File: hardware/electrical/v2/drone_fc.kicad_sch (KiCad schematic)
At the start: 33 parts, among them J1 Cortex_SWD_10P, J2 ESC_4IN1_JST_SH, U1 TLV75533PDBVR, U2 LMR50410_Buck, U3 MDBT53-P1M, U4 ICM-42688-P

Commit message: j2: adopt the KiCad library footprint for the ESC connector
Switches J2 from the hand-made drone_fc_v2_footprints copy to KiCad's
Connector_JST:JST_SH_SM08B-SRSS-TB_1x08-1MP_P1.00mm_Horizontal.

The two disagreed on the mechanical retention pads: signal-to-MP separation
of 3.25 mm against 3.875 mm, with the MP pads 0.4 mm further out in the
library version. Those pads take the load every time the ESC harness is
unplugged, so the geometry matters. JST's own drawing could not be read
programmatically to arbitrate, but provenance is decisive - the library
footprint is machine-generated from eSH.pdf by kicad-footprint-generator and
peer-reviewed, whereas ours came from the same CopperPilot generation that
produced mislabelled symbol pins, a self-intersecting courtyard and an
unverified BOM. The swap also brings the manufacturer STEP model, which the
custom footprint lacked.

Also links TP1-TP4 to their schematic symbols. Those pads were created
directly in the board file before the matching TestPoint symbols existed, so
they carried no path and Update PCB from Schematic kept offering to add four
duplicates.

This is an intermediate state with known errors. Fitting the reviewed
footprint revealed that the connector opens toward the board centre rather
than out through the edge, so it still needs rotating 180 degrees and moving
to y ~88.6. Until then DRC reports eight board-edge clearance errors (pads
0.425 mm from the edge against a 0.5 mm rule) and a courtyard overlap with
TP2, all within the area that rework will cover. ERC is clean and no nets
are unconnected.
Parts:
- J2: footprint drone_fc_v2_footprints:JST_SH_SM08B-SRSS-TB_1x08-1MP_P1.00mm_Horizontal -> Connector_JST:JST_SH_SM08B-SRSS-TB_1x08-1MP_P1.00mm_Horizontal
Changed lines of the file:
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@@
 			)
 		)
-		(property "Footprint" "drone_fc_v2_footprints:JST_SH_SM08B-SRSS-TB_1x08-1MP_P1.00mm_Horizontal"
+		(property "Footprint" "Connector_JST:JST_SH_SM08B-SRSS-TB_1x08-1MP_P1.00mm_Horizontal"
 			(at 342.9 195.58 0)
 			(hide yes)

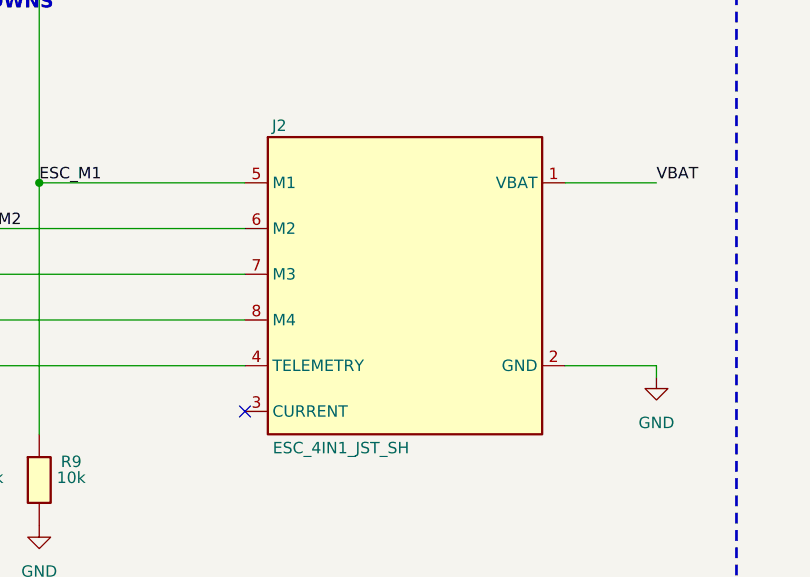
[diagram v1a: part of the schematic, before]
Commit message: j2: reverse connector pin numbering to match the ESC harness
The board-side pinout is now pin 1 = M4 through pin 8 = VBAT, reversed from
the JST convention the parts-list documents. This matches the custom harness
as measured: with the socket held open-end toward you, VBAT sits on the right,
which places it on the left-hand pad once the header is rotated to open
outward. Pin numbering is reversed in the symbol rather than the footprint, so
the schematic drawing and its wiring are unchanged and only the pad mapping
moves.

J2 is rotated 180 degrees so the connector opens out through the top board
edge rather than into the board interior. The opening direction was settled by
rendering the manufacturer STEP model - the 2D pads and courtyard are
ambiguous, and reasoning from them produced two wrong conclusions before the
render.

Intermediate state. Re-routing around the rotated connector is unfinished:
three nets are open in the buck area (+4V, C5 ground, R2 feedback) and both J2
mounting pads sit 0.235 mm from the board edge against a 0.5 mm rule, so the
connector needs nudging inboard. ERC is clean and the remaining twelve DRC
findings are silkscreen only.

Committed mid-edit because KiCad crashed; the files were checked for damage
first and both parse cleanly.
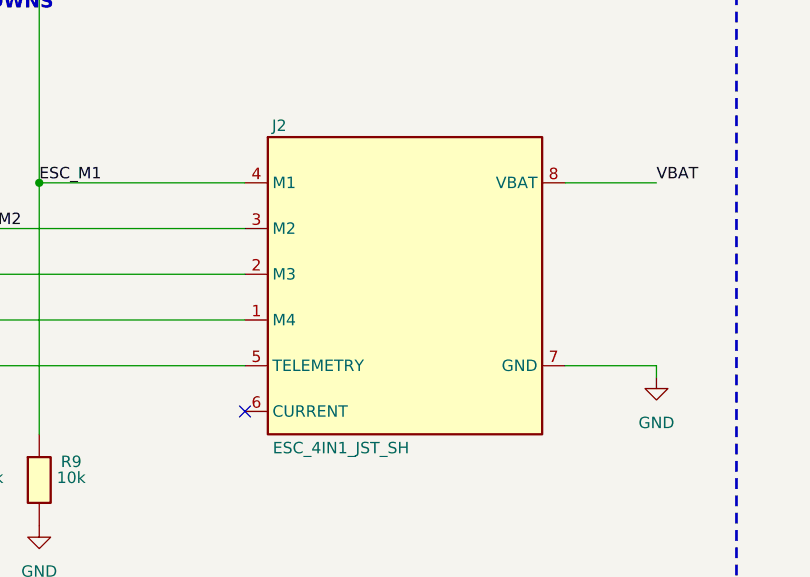
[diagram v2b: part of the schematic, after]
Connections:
- net ESC_M1: now also J2.4 (M1); no longer J2.5 (M1)
- net ESC_M2: now also J2.3 (M2); no longer J2.6 (M2)
- net ESC_M3: now also J2.2 (M3); no longer J2.7 (M3)
- net ESC_M4: now also J2.1 (M4); no longer J2.8 (M4)
- net ESC_TLM: now also J2.5 (TELEMETRY); no longer J2.4 (TELEMETRY)
- net GND: now also J2.7 (GND); no longer J2.2 (GND)
- net VBAT: now also J2.8 (VBAT); no longer J2.1 (VBAT)

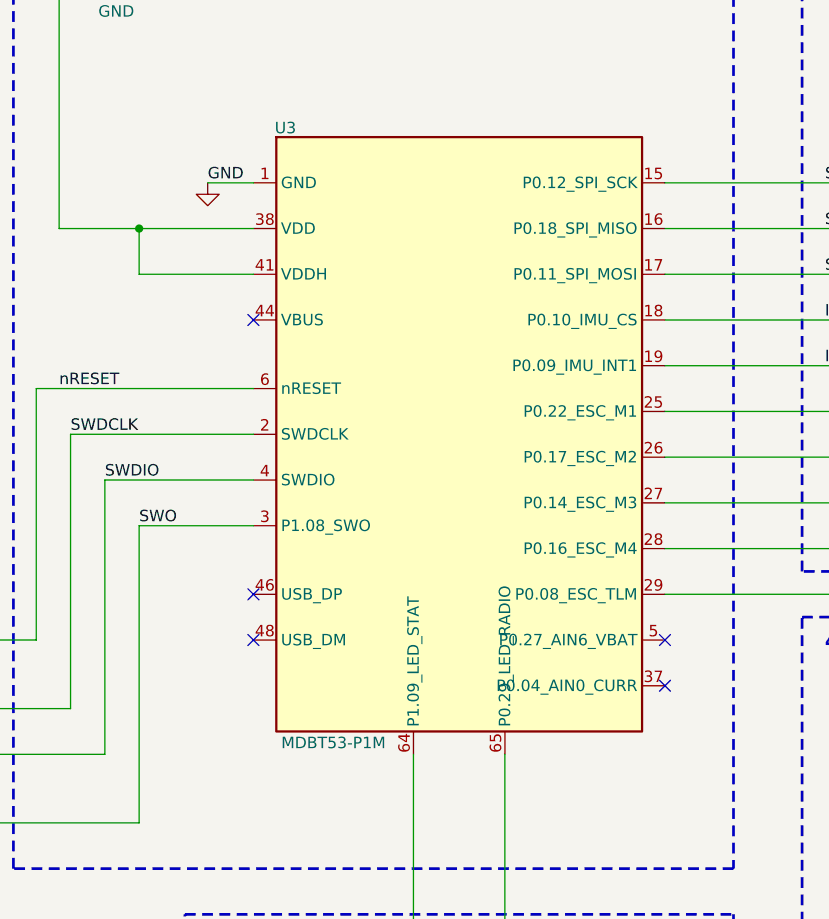
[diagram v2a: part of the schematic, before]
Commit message: u3,j2: fix pin assignments, reroute, and re-center the IMU
Corrects several MDBT53/nRF5340 pin assignments against the module's
official pin table (Raytac spec section 2.5), and reroutes accordingly:

- Add the three missing GND pins (24, 42, 61) to the MDBT53_P1M symbol.
  Only pin 1 was previously declared; the other three physical ground
  pads were floating on the board. Pin 42 was first mis-added as 43
  (P1.01, a GPIO) and corrected after cross-checking the datasheet.
- Move ESC_M3/ESC_M4 off pin 27 (inconveniently interior) onto 28/30,
  fixing a resulting crossed wire: swapping the label text alone
  didn't move the connection, since these are direct point-to-point
  wires to J2, not label-joined nets - the wire geometry had to move,
  not just its annotation.
- Reverse the motor pin order on the MCU side (M1<-30, M2<-28, M3<-26,
  M4<-25) for routing convenience, without touching the J2 wiring:
  only the silicon pin driving each already-fixed destination changed.
- Move LED_STAT/LED_RADIO off pin 58 (DECR, a regulator decoupling
  pin, not GPIO) onto 60/56.
- Move SPI_SCK/MOSI/CS/INT1 off the inner castellation row onto the
  outer row (20/18/22/14), keeping MISO at 16.
- Widen the antenna keepout to the full board width per the module
  design guide, not just the antenna footprint.
- Re-center U4 (ICM-42688-P) on the board.

Board fully re-routed for the above (0 unconnected items). ERC clean.
Remaining DRC output is expected in-progress noise: two standard-library
footprint version-drift warnings (R6/R7) and courtyard/tuning notices.
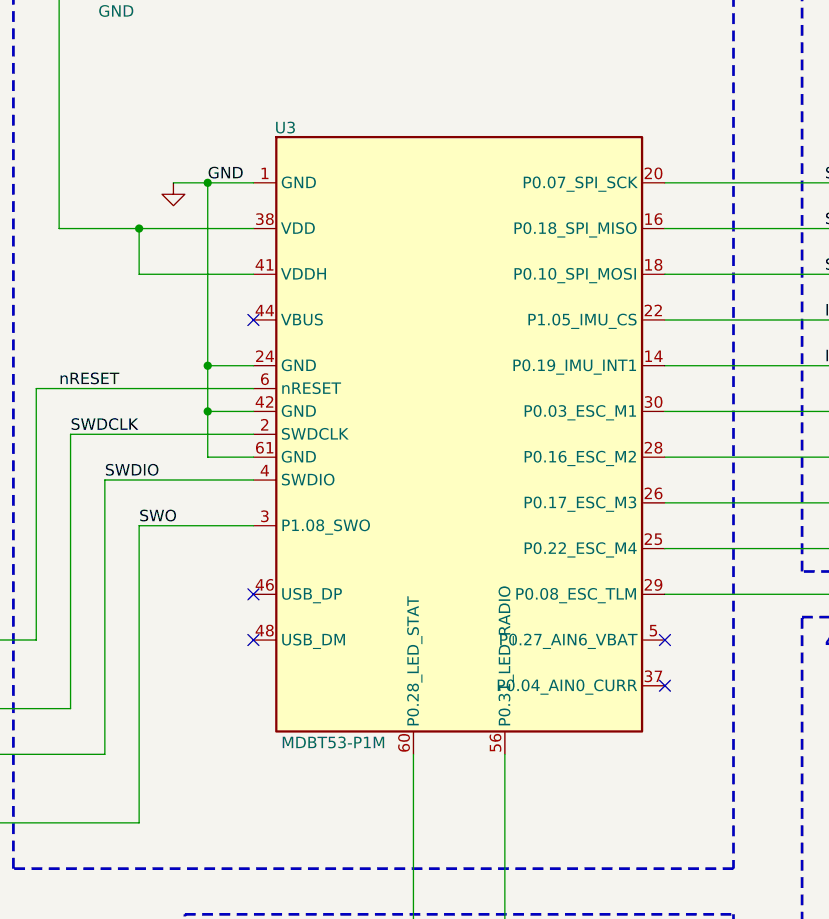
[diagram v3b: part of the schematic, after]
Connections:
- net ESC_M1: now also U3.30 (P0.03_ESC_M1); no longer U3.25 (P0.22_ESC_M1)
- net ESC_M2: now also U3.28 (P0.16_ESC_M2); no longer U3.26 (P0.17_ESC_M2)
- net ESC_M3: now also U3.26 (P0.17_ESC_M3); no longer U3.27 (P0.14_ESC_M3)
- net ESC_M4: now also U3.25 (P0.22_ESC_M4); no longer U3.28 (P0.16_ESC_M4)
- net GND: now also U3.24 (GND), U3.42 (GND), U3.61 (GND)
- net IMU_CS: now also U3.22 (P1.05_IMU_CS); no longer U3.18 (P0.10_IMU_CS)
- net IMU_INT1: now also U3.14 (P0.19_IMU_INT1); no longer U3.19 (P0.09_IMU_INT1)
- net SPI_MOSI: now also U3.18 (P0.10_SPI_MOSI); no longer U3.17 (P0.11_SPI_MOSI)
- net SPI_SCK: now also U3.20 (P0.07_SPI_SCK); no longer U3.15 (P0.12_SPI_SCK)
- net at D1.1 (A): now also U3.60 (P0.28_LED_STAT); no longer U3.64 (P1.09_LED_STAT)
- net at D2.1 (A): now also U3.56 (P0.31_LED_RADIO); no longer U3.65 (P0.29_LED_RADIO)
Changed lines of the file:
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@@
 	)
 	(junction
+		(at 187.96 139.7)
+		(diameter 0)
+		(color 0 0 0 0)
+	)
+	(junction
 		(at 360.68 129.54)
 		(diameter 0.9144)
@@
 	)
 	(junction
+		(at 187.96 134.62)
+		(diameter 0)
+		(color 0 0 0 0)
+	)
+	(junction
+		(at 187.96 114.3)
+		(diameter 0)
+		(color 0 0 0 0)
+	)
+	(junction
 		(at 373.38 129.54)
 		(diameter 0.9144)
@@
 	(wire
 		(pts
+			(xy 187.96 134.62) (xy 187.96 114.3)
+		)
+		(stroke
+			(width 0)
+			(type default)
+		)
+	)
+	(wire
+		(pts
 			(xy 350.52 137.16) (xy 360.68 137.16)
 		)
@@
 	(wire
 		(pts
+			(xy 184.15 114.3) (xy 187.96 114.3)
+		)
+		(stroke
+			(width 0)
+			(type default)
+		)
+	)
+	(wire
+		(pts
 			(xy 168.91 137.16) (xy 193.04 137.16)
 		)
@@
 	(wire
 		(pts
+			(xy 193.04 139.7) (xy 187.96 139.7)
+		)
+		(stroke
+			(width 0)
+			(type default)
+		)
+	)
+	(wire
+		(pts
 			(xy 93.98 165.1) (xy 168.91 165.1)
 		)
@@
 	(wire
 		(pts
+			(xy 187.96 139.7) (xy 187.96 144.78)
+		)
+		(stroke
+			(width 0)
+			(type default)
+		)
+	)
+	(wire
+		(pts
 			(xy 274.32 200.66) (xy 274.32 154.94)
 		)
@@
 	(wire
 		(pts
-			(xy 171.45 119.38) (xy 180.34 119.38)
+			(xy 187.96 114.3) (xy 193.04 114.3)
 		)
 		(stroke
@@
 	(wire
 		(pts
-			(xy 187.96 114.3) (xy 193.04 114.3)
+			(xy 171.45 119.38) (xy 180.34 119.38)
 		)
 		(stroke
@@
 	(wire
 		(pts
+			(xy 193.04 134.62) (xy 187.96 134.62)
+		)
+		(stroke
+			(width 0)
+			(type default)
+		)
+	)
+	(wire
+		(pts
 			(xy 172.72 142.24) (xy 193.04 142.24)
 		)
@@
 	(wire
 		(pts
+			(xy 193.04 144.78) (xy 187.96 144.78)
+		)
+		(stroke
+			(width 0)
+			(type default)
+		)
+	)
+	(wire
+		(pts
 			(xy 238.76 160.02) (xy 264.16 160.02)
 		)
@@
 	(wire
 		(pts
+			(xy 187.96 134.62) (xy 187.96 139.7)
+		)
+		(stroke
+			(width 0)
+			(type default)
+		)
+	)
+	(wire
+		(pts
 			(xy 220.98 177.8) (xy 220.98 203.2)
 		)
@@
 	(symbol
 		(lib_id "power:GND")
-		(at 187.96 114.3 0)
+		(at 184.15 114.3 0)
 		(unit 1)
 		(body_style 1)
@@
 		(dnp no)
 		(property "Reference" "#PWR011"
-			(at 187.96 120.65 0)
+			(at 184.15 120.65 0)
 			(hide yes)
 			(show_name no)
@@
 		)
 		(property "Value" "GND"
-			(at 183.388 110.236 0)
+			(at 179.578 110.236 0)
 			(hide yes)
 			(show_name no)
@@
 		)
 		(property "Footprint" ""
-			(at 187.96 114.3 0)
+			(at 184.15 114.3 0)
 			(hide yes)
 			(show_name no)
@@
 		)
 		(property "Datasheet" ""
-			(at 187.96 114.3 0)
+			(at 184.15 114.3 0)
 			(hide yes)
 			(show_name no)
@@
 		)
 		(property "Description" "Power symbol creates a global label with name \"GND\" , ground"
-			(at 187.96 114.3 0)
+			(at 184.15 114.3 0)
 			(hide yes)
 			(show_name no)
@@
 		(pin "6"
 		)
-		(pin "27"
+		(pin "30"
 		)
 		(pin "25"
@@
 		(pin "28"
 		)
-		(pin "15"
+		(pin "20"
 		)
 		(pin "16"
 		)
-		(pin "17"
+		(pin "14"
 		)
 		(pin "18"
 		)
-		(pin "19"
+		(pin "22"
 		)
-		(pin "65"
+		(pin "60"
 		)
-		(pin "64"
+		(pin "56"
 		)
 		(pin "48"
@@
 		(pin "37"
 		)
+		(pin "24"
+		)
+		(pin "42"
+		)
+		(pin "61"
+		)
 		(instances

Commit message: hardware: replace redundant custom schematic symbols
Use stock KiCad symbols for passives, regulators and connectors, and correct the LED symbol polarity. Preserve the manufactured PCB and all other electrical connections.

Review the cosmetic wiring edits, separate the accidental ESC_M2/ESC_M3 junction, and remove a dangling ground stub. Document the module reset pull-up ERC exception. Netlist comparison passes; only the pre-existing module library mismatch remains.
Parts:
- C1, C10, C2, C3, C4, C5, C6, C7, C8, C9: symbol drone_fc_v2_symbols:Capacitor -> Device:C
- D1, D2: symbol drone_fc_v2_symbols:LED_Status -> Device:LED
- J1: symbol drone_fc_v2_symbols:Cortex_SWD_10P -> Connector:Conn_ARM_JTAG_SWD_10
- J2: symbol drone_fc_v2_symbols:ESC_4in1_Connector -> Connector_Generic:Conn_01x08
- L1: symbol drone_fc_v2_symbols:Inductor -> Device:L
- R1, R2, R3, R4, R5, R6, R7, R8, R9: symbol drone_fc_v2_symbols:Resistor -> Device:R
- TVS1: symbol drone_fc_v2_symbols:Diode_TVS -> Diode:SMAJ24A
- U1: symbol drone_fc_v2_symbols:TLV75533PDBVR -> Regulator_Linear:TLV75533PDBV
- U2: symbol drone_fc_v2_symbols:LMR50410_Buck -> Regulator_Switching:LMR50410
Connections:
- net at D1.1 (K): now also R3.1; no longer U3.60 (P0.28_LED_STAT)
- net at D1.2 (A): now also U3.60 (P0.28_LED_STAT); no longer R3.1
- net at D2.1 (K): now also R4.1; no longer U3.56 (P0.31_LED_RADIO)
- net at D2.2 (A): now also U3.56 (P0.31_LED_RADIO); no longer R4.1
- no-connect marks 8 -> 10
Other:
- moved on the sheet: C2, C3, C4, J2, TP1, TP4

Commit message: hardware: complete the MDBT53-P1M module symbol
Expose all 65 pads using the Raytac Rev. E pin map and manufacturer GPIO names. Keep existing wired geometry, add units for remaining GPIO and regulator pins, and synchronise the library and schematic copies.

Mark unused pads explicitly unconnected and document normal-voltage LDO assumptions. Verify original connectivity and component fields are preserved, all added pads are unconnected on the unchanged PCB, and ERC reports no errors or warnings.
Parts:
- added unit 3 of U3
- added unit 2 of U3
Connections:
- net LED_STATUS: now reaches D1.2 (A), U3.60 (P0.28)
- net LED_RADIO: now reaches D2.2 (A), U3.56 (P0.31)
- no-connect marks 10 -> 48
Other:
- note added: "U3C: regulator pins unused in normal-voltage LDO mode. VDD and VDDH tied to 3.3 V; DC/DC must remain disabled. Raytac Rev. E, section 8.1.1."
